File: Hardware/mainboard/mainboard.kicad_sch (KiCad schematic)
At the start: 25 parts, among them J1 Conn_01x18_Pin, J2 Conn_01x11_Pin, J3 Conn_01x04_Pin, J4 USB_B_Micro, SW1 SW_SPDT, U1 STM32L151CBTxA, U2 AMS1117-3.3, Y1 16MHz

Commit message: more work on pcb
finished house season 2 and made decent progress (i think) on the pcb. if it is bad ill see tomorrow lol
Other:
- title: (none) -> L151 breakout board
- moved on the sheet: C1, C10, C11, C12, C2, C3, C4, C5, C6, C7, C8, C9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

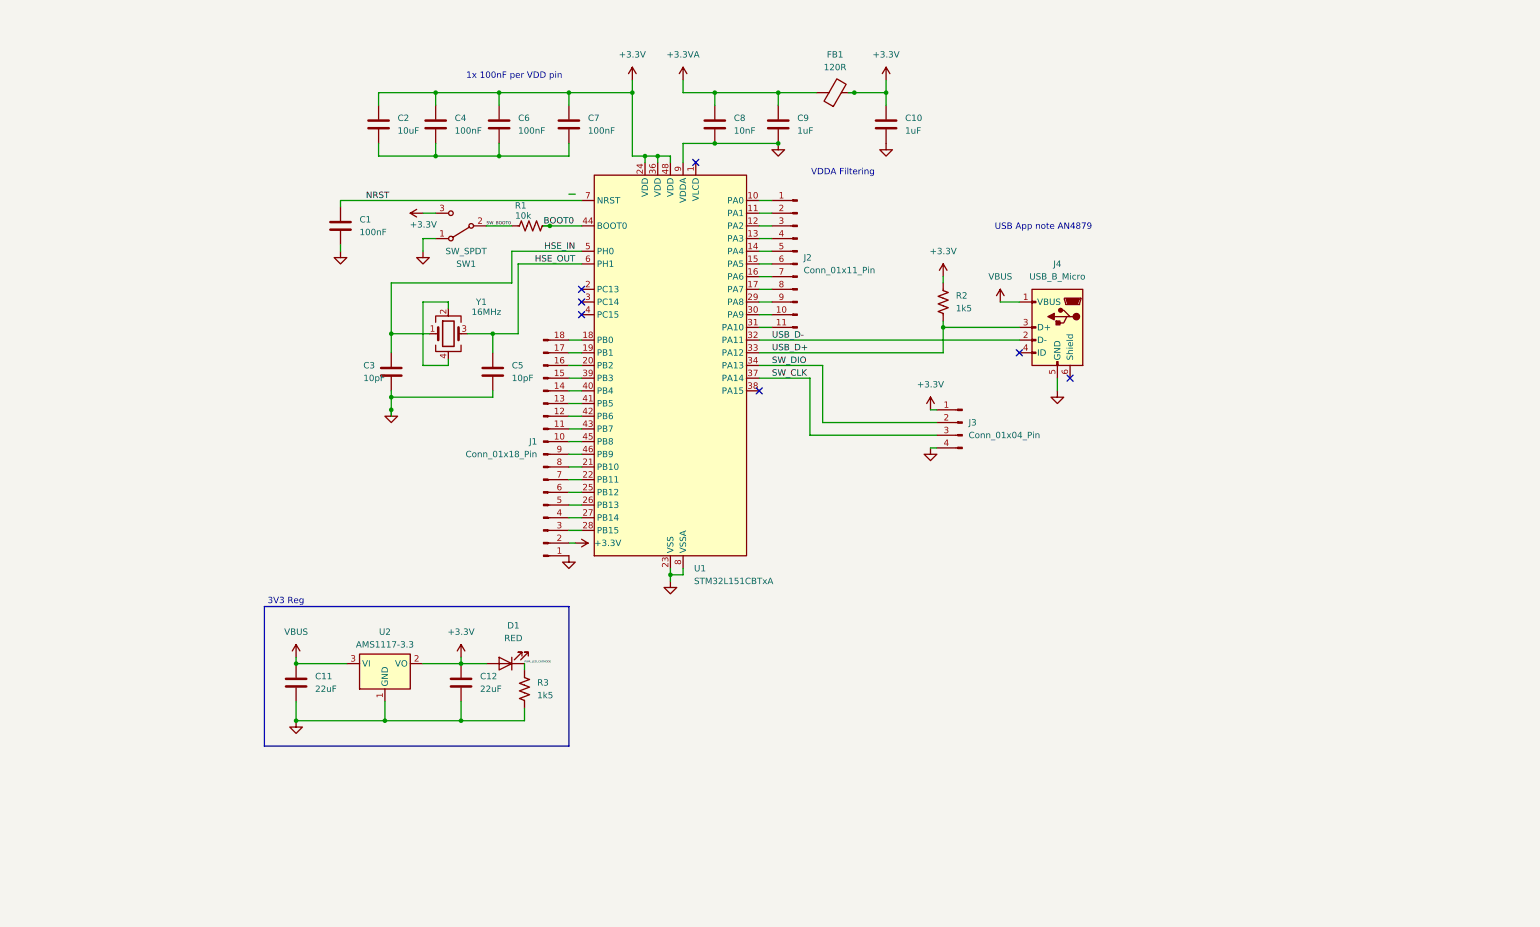
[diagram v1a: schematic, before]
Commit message: began work on mainboard
mostly schematic but i did assign footprints (if you even consider that to be working on the pcb)
power in from usb and ONLY power from usb - no dp just vbus and gnd. still dnt know what cc or shield is but i can figure that out later
jtag and usb-ttl for programming. will not be powered by usb while programmed.
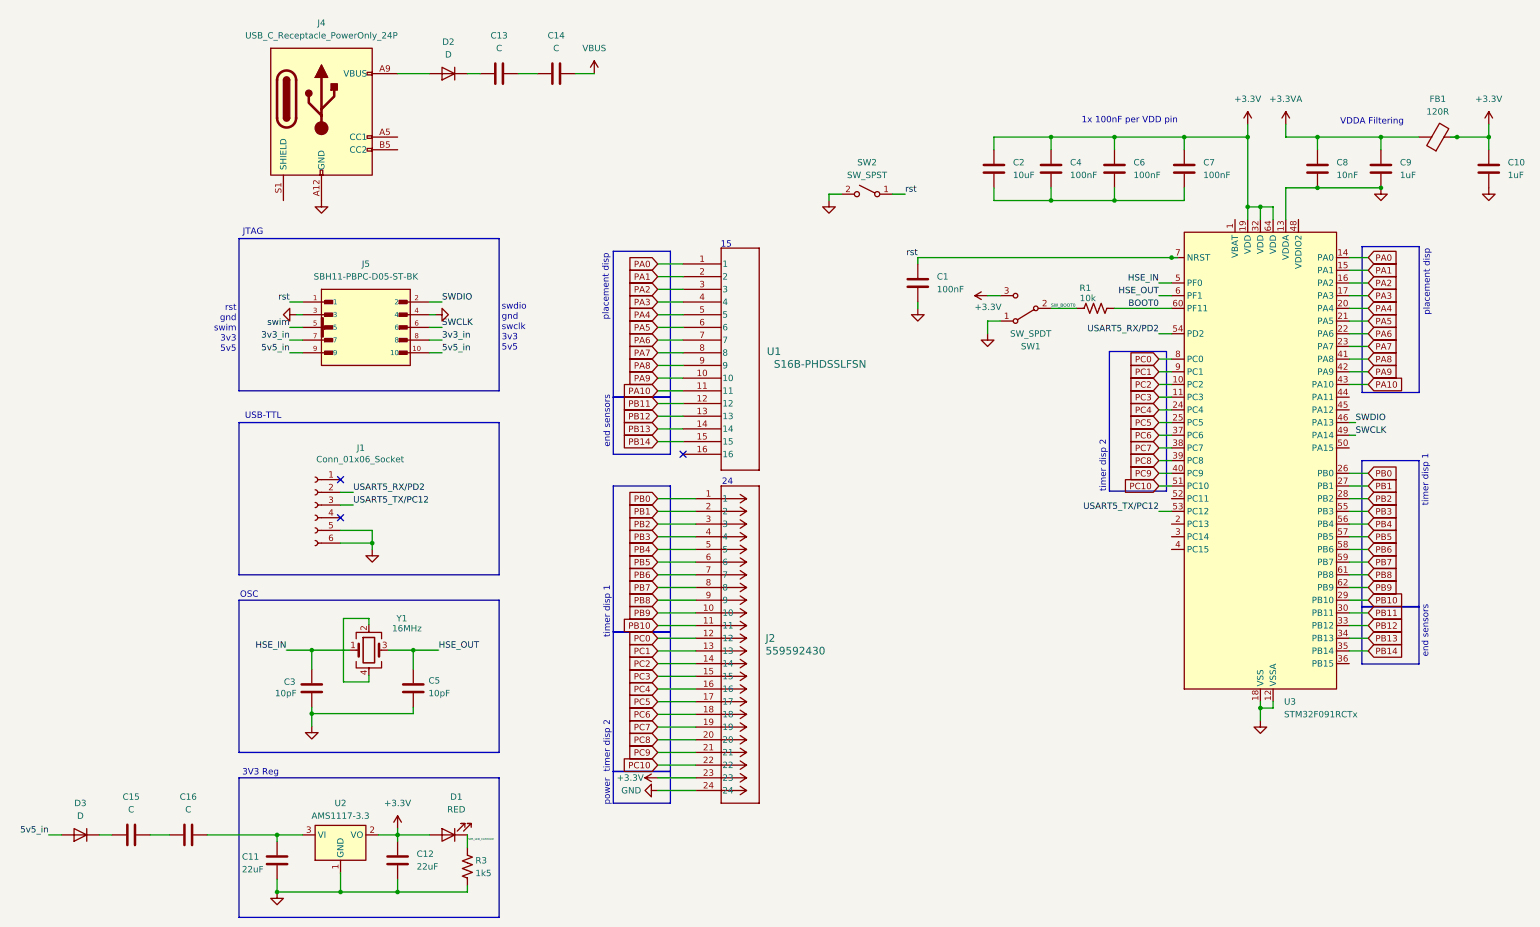
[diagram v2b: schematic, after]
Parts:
- removed J1: Conn_01x18_Pin, symbol Connector:Conn_01x18_Pin
- removed J2: Conn_01x11_Pin, symbol Connector:Conn_01x11_Pin
- removed J3: Conn_01x04_Pin, symbol Connector:Conn_01x04_Pin
- removed J4: USB_B_Micro, symbol Connector:USB_B_Micro
- removed R2: 1k5, symbol Device:R_US
- removed U1: STM32L151CBTxA, Package_QFP:LQFP-48_7x7mm_P0.5mm, symbol MCU_ST_STM32L1:STM32L151CBTxA
- added C13, C14, C15, C16: C, symbol Device:C
- added D2, D3: D, symbol Device:D
- added J1: Conn_01x06_Socket, jtag:SULLINS_SBH11-PBPC-D05-ST-BK, symbol Connector:Conn_01x06_Socket
- added J2: 559592430, 24pos 2mm:CONN24_559592430_MOL, symbol CONN HEADER 24POS 2MM:559592430
- added J4: USB_C_Receptacle_PowerOnly_24P, symbol Connector:USB_C_Receptacle_PowerOnly_24P
- added J5: SBH11-PBPC-D05-ST-BK, SBH11-PBPC-D05-ST-BK:SULLINS_SBH11-PBPC-D05-ST-BK, symbol jtag:SBH11-PBPC-D05-ST-BK
- added SW2: SW_SPST, symbol Switch:SW_SPST
- added U1: S16B-PHDSSLFSN, 16pos 2mm:S16B-PHDSSLFSN_JST, symbol CONN HEADER 16POS 2MM:S16B-PHDSSLFSN
- added U3: STM32F091RCTx, Package_QFP:LQFP-64_10x10mm_P0.5mm, symbol MCU_ST_STM32F0:STM32F091RCTx
- C1, C10, C11, C12, C2, C3, C4, C5, C6, C7, C8, C9: footprint (none) -> Capacitor_SMD:C_0805_2012Metric
- D1: footprint (none) -> Diode_SMD:D_0805_2012Metric
- FB1, R1, R3: footprint (none) -> Resistor_SMD:R_0805_2012Metric_Pad1.20x1.40mm_HandSolder
- U2: footprint Package_TO_SOT_SMD:SOT-223-3_TabPin2 -> 3v3reg:SOT23-BEC
- Y1: footprint (none) -> crystal smd:OSC_ECS-2520S25-250-FN-TR
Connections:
- net +3.3V: now also J2.23, U3.19 (VDD), U3.32 (VDD), U3.64 (VDD)
- net BOOT0: now also U3.60 (PF11)
- net GND: now also J1.5 (Pin_5), J1.6 (Pin_6), J2.24, J4.A1 (GND), J4.A12 (GND), J4.B1 (GND), J4.B12 (GND), J5.3, J5.4, SW2.2 (B), U3.12 (VSSA), U3.13 (VDDA), U3.18 (VSS), U3.31 (VSS), U3.47 (VSS), U3.63 (VSS)
- net HSE_IN: now also U3.5 (PF0)
- net HSE_OUT: now also U3.6 (PF1)
- net VBUS: now also C14.2; no longer C11.1, U2.3 (VI)
- net NRST renamed rst
- net rst: now also J5.1, SW2.1 (A), U3.7 (NRST)
- new net: C13.2, C14.1
- new net: C15.1, D3.1 (K)
- new net: C11.1, C16.2, U2.3 (VI)
- new net: C15.2, C16.1
- new net: D2.2 (A), J4.A4 (VBUS), J4.A9 (VBUS), J4.B4 (VBUS), J4.B9 (VBUS)
- new net: C13.1, D2.1 (K)
- new net 3v3_in: J5.7, J5.8
- new net 5v5_in: D3.2 (A), J5.10, J5.9
- new net PA0: U1.1, U3.14 (PA0)
- new net PA1: U1.2, U3.15 (PA1)
- new net PA10: U1.11, U3.43 (PA10)
- new net PA2: U1.3, U3.16 (PA2)
- new net PA3: U1.4, U3.17 (PA3)
- new net PA4: U1.5, U3.20 (PA4)
- new net PA5: U1.6, U3.21 (PA5)
- new net PA6: U1.7, U3.22 (PA6)
- new net PA7: U1.8, U3.23 (PA7)
- new net PA8: U1.9, U3.41 (PA8)
- new net PA9: U1.10, U3.42 (PA9)
- new net PB0: J2.1, U3.26 (PB0)
- new net PB1: J2.2, U3.27 (PB1)
- new net PB10: J2.11, U3.29 (PB10)
- new net PB11: U1.12, U3.30 (PB11)
- new net PB12: U1.13, U3.33 (PB12)
- new net PB13: U1.14, U3.34 (PB13)
- new net PB14: U1.15, U3.35 (PB14)
- new net PB2: J2.3, U3.28 (PB2)
- new net PB3: J2.4, U3.55 (PB3)
- new net PB4: J2.5, U3.56 (PB4)
- new net PB5: J2.6, U3.57 (PB5)
- new net PB6: J2.7, U3.58 (PB6)
- new net PB7: J2.8, U3.59 (PB7)
- new net PB8: J2.9, U3.61 (PB8)
- new net PB9: J2.10, U3.62 (PB9)
- new net PC0: J2.12, U3.8 (PC0)
- new net PC1: J2.13, U3.9 (PC1)
- new net PC10: J2.22, U3.51 (PC10)
- new net PC2: J2.14, U3.10 (PC2)
- new net PC3: J2.15, U3.11 (PC3)
- new net PC4: J2.16, U3.24 (PC4)
- new net PC5: J2.17, U3.25 (PC5)
- new net PC6: J2.18, U3.37 (PC6)
- new net PC7: J2.19, U3.38 (PC7)
- new net PC8: J2.20, U3.39 (PC8)
- new net PC9: J2.21, U3.40 (PC9)
- new net SWCLK: J5.6, U3.49 (PA14)
- new net SWDIO: J5.2, U3.46 (PA13)
- new net USART5_RX/PD2: J1.2 (Pin_2), U3.54 (PD2)
- new net USART5_TX/PC12: J1.3 (Pin_3), U3.53 (PC12)
- new net swim: J5.5
- no-connect marks 7 -> 3
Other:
- note added: "15"
- note added: "24"
- note added: "JTAG"
- note added: "OSC"
- note added: "USB-TTL"
- note added: "end sensors"
- note added: "placement disp"
- note added: "power"
- note added: "rst gnd swim 3v3 5v5"
- note added: "swdio gnd swclk 3v3 5v5"
- note added: "timer disp 1"
- note added: "timer disp 2"
- note removed: "USB App note AN4879"
- moved on the sheet: C11, C12, D1, R3, U2

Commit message: updated mainboard schematic
organization and power
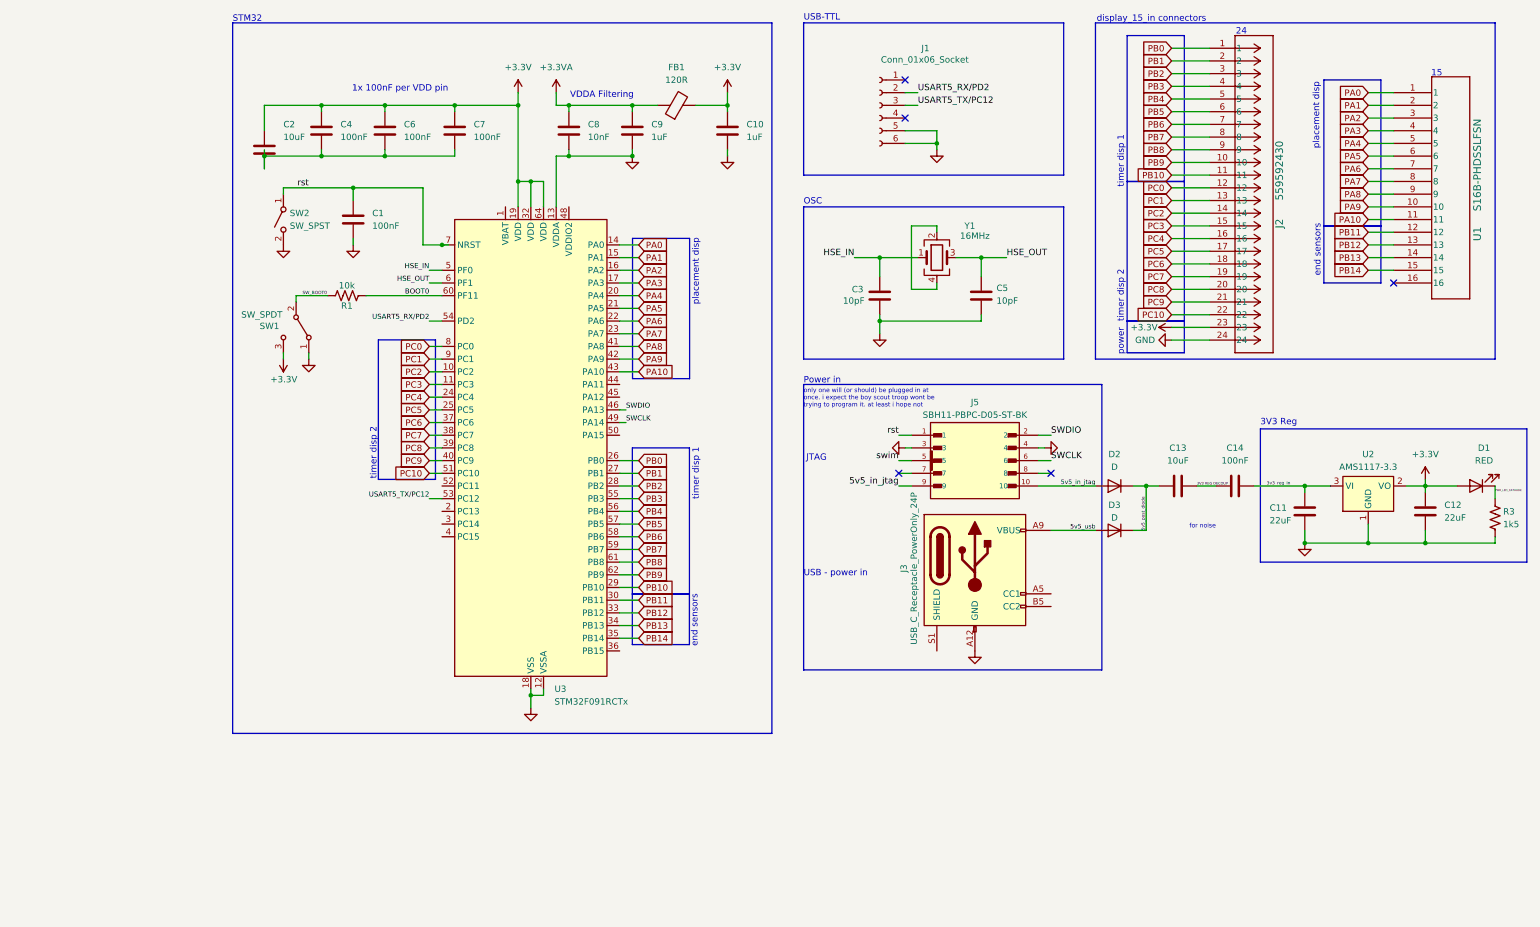
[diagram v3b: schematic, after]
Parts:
- removed C15, C16: C, symbol Device:C
- removed J4: USB_C_Receptacle_PowerOnly_24P, symbol Connector:USB_C_Receptacle_PowerOnly_24P
- added J3: USB_C_Receptacle_PowerOnly_24P, symbol Connector:USB_C_Receptacle_PowerOnly_24P
- C13: value C -> 10uF; footprint (none) -> Capacitor_SMD:C_0805_2012Metric
- C14: value C -> 100nF; footprint (none) -> Capacitor_SMD:C_0805_2012Metric
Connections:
- net VBUS is gone; now on net 3v3_reg_in: C14.2
- net GND: now also J3.A1 (GND), J3.A12 (GND), J3.B1 (GND), J3.B12 (GND)
- net 3V3 REG DECOUP: now reaches C13.2, C14.1
- net 5v5_post_diode: now reaches D3.1 (K)
- net 5v5_post_diode: now also C13.1, D2.1 (K)
- net 3v3_reg_in: now reaches C11.1, U2.3 (VI)
- net 5v5_in_jtag: now reaches D2.2 (A)
- net 5v5_in_jtag: now also J5.10, J5.9
- net 3v3_in: no longer names the net of J5.7
- net 3v3_in: no longer J5.8
- removed net 5v5_in: D3.2 (A), J5.10, J5.9
- new net 5v5_usb: D3.2 (A), J3.A4 (VBUS), J3.A9 (VBUS), J3.B4 (VBUS), J3.B9 (VBUS)
- no-connect marks 3 -> 5
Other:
- note added: "Power in"
- note added: "STM32"
- note added: "USB - power in"
- note added: "display_15_in connectors"
- note added: "for noise"
- note added: "only one will (or should) be plugged in at once. i expect the boy scout troop wont be trying to program it. at least i hope not"
- note removed: "rst gnd swim 3v3 5v5"
- note removed: "swdio gnd swclk 3v3 5v5"
- title: L151 breakout board -> F091RCT6 mainboard
- moved on the sheet: C1, C10, C11, C12, C2, C3, C4, C5, C6, C7, C8, C9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

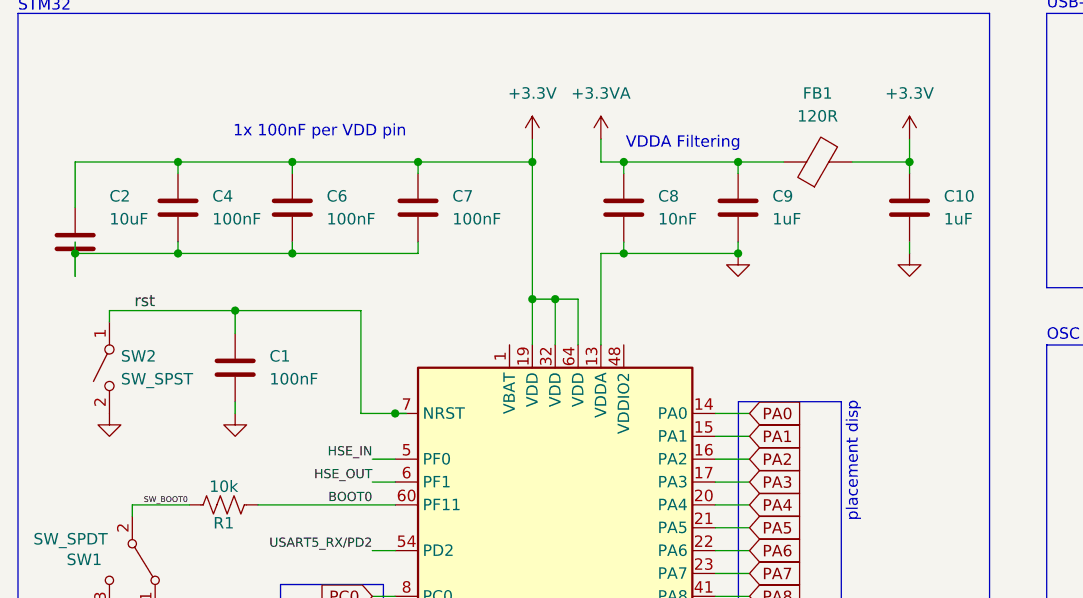
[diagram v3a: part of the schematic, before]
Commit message: forgor race reset button
theres a reset on the board and a reset on the side for them to hit to clear it for the next race
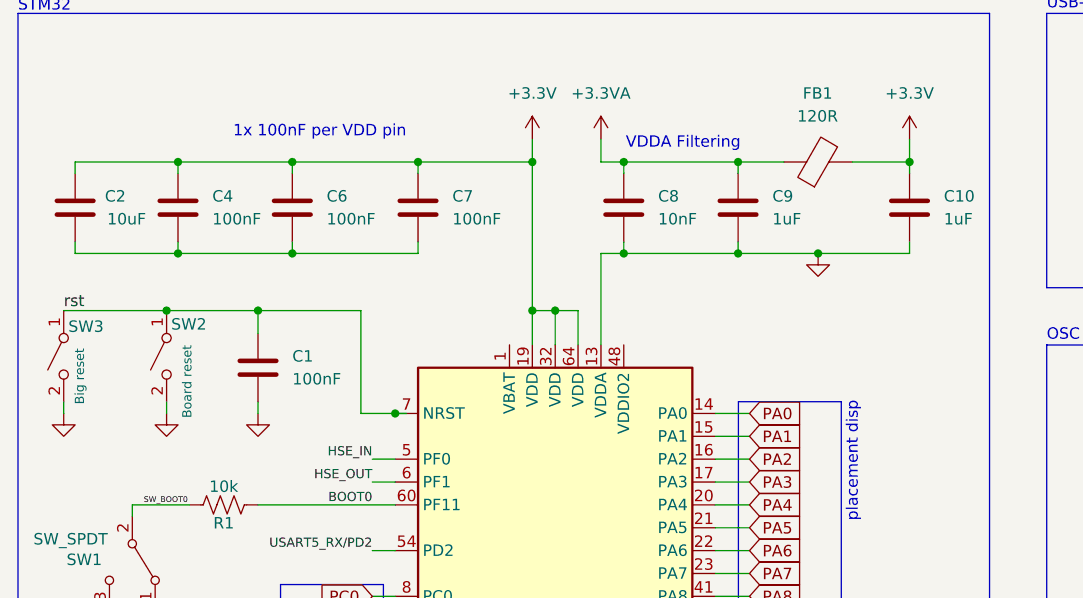
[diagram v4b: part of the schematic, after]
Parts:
- added SW3: Big reset, symbol Switch:SW_SPST
- SW2: value SW_SPST -> Board reset
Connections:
- net GND: now also SW3.2 (B)
- net rst: now also SW3.1 (A)
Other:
- moved on the sheet: C1, SW2
